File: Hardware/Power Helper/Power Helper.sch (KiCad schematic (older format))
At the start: 13 parts, among them J1 USB_C_Receptacle_Power_Only, J2 Conn_02x02_Odd_Even, J3 Conn_02x02_Odd_Even, SW1 SW_SPDT, SW2 SW_SPDT, SW3 SW_SPDT, U1 AZ1117-3.3

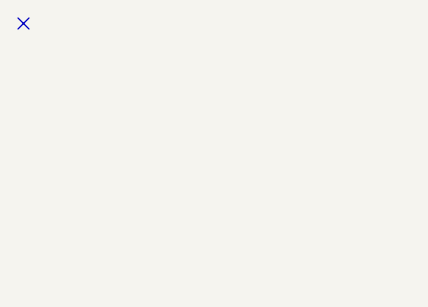
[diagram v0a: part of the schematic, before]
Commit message: JLC fix
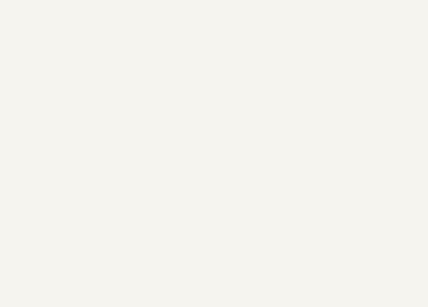
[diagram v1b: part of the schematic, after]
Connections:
- no-connect marks 2 -> 1
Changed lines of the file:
@@
 	3450 3300 3450 3400
 NoConn ~ 3450 3200
-NoConn ~ -1950 950
 $EndSCHEMATC

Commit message: Prepare for production
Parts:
- C1: LCSC (none) -> C7171
- C2: LCSC (none) -> C129272
- D1: LCSC (none) -> C2293
- J1: LCSC (none) -> C283540
- R1, R2: LCSC (none) -> C27834
- R3: LCSC (none) -> C17630
- SW1, SW2, SW3: Sparkfun (none) -> COM-10860
- U1: LCSC (none) -> C108492
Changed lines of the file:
@@
 F 2 "Power Helper:CUI_UJC-HP-3-SMT-TR" H 2100 3900 50  0001 C CNN
 F 3 "" H 2100 3900 50  0001 C CNN
+F 4 "C283540" H 1950 3900 50  0001 C CNN "LCSC"
 	1    1950 3900
 	1    0    0    -1
@@
 F 2 "Resistor_SMD:R_0805_2012Metric" V 2880 3900 50  0001 C CNN
 F 3 "~" H 2950 3900 50  0001 C CNN
+F 4 "C27834" H 2950 3900 50  0001 C CNN "LCSC"
 	1    2950 3900
 	1    0    0    -1
@@
 F 2 "Resistor_SMD:R_0805_2012Metric" V 3180 3900 50  0001 C CNN
 F 3 "~" H 3250 3900 50  0001 C CNN
+F 4 "C27834" H 3250 3900 50  0001 C CNN "LCSC"
 	1    3250 3900
 	1    0    0    -1
@@
 F 2 "Resistor_SMD:R_0805_2012Metric" V 3630 3900 50  0001 C CNN
 F 3 "~" H 3700 3900 50  0001 C CNN
+F 4 "C17630" H 3700 3900 50  0001 C CNN "LCSC"
 	1    3700 3900
 	1    0    0    -1
@@
 F 2 "LED_SMD:LED_0805_2012Metric" H 3700 3550 50  0001 C CNN
 F 3 "~" H 3700 3550 50  0001 C CNN
+F 4 "C2293" V 3700 3550 50  0001 C CNN "LCSC"
 	1    3700 3550
 	0    -1   -1   0
@@
 F 2 "Package_TO_SOT_SMD:SOT-223-3_TabPin2" H 4650 3500 50  0001 C CNN
 F 3 "https://www.diodes.com/assets/Datasheets/AZ1117.pdf" H 4750 3050 50  0001 C CNN
+F 4 "C108492" H 4650 3300 50  0001 C CNN "LCSC"
 	1    4650 3300
 	1    0    0    -1
@@
 F 2 "Capacitor_SMD:C_1206_3216Metric" H 4238 3750 50  0001 C CNN
 F 3 "~" H 4200 3900 50  0001 C CNN
+F 4 "C7171" H 4200 3900 50  0001 C CNN "LCSC"
 	1    4200 3900
 	1    0    0    -1
@@
 F 2 "Capacitor_SMD:C_1206_3216Metric" H 5138 3750 50  0001 C CNN
 F 3 "~" H 5100 3900 50  0001 C CNN
+F 4 "C129272" H 5100 3900 50  0001 C CNN "LCSC"
 	1    5100 3900
 	1    0    0    -1
@@
 F 2 "Switches:SWITCH_SPST_SMD_A" H 7550 3400 50  0001 C CNN
 F 3 "~" H 7550 3400 50  0001 C CNN
+F 4 "COM-10860" H 7550 3400 50  0001 C CNN "Sparkfun"
 	1    7550 3400
 	-1   0    0    -1
@@
 F 2 "Switches:SWITCH_SPST_SMD_A" H 7550 4000 50  0001 C CNN
 F 3 "~" H 7550 4000 50  0001 C CNN
+F 4 "COM-10860" H 7550 4000 50  0001 C CNN "Sparkfun"
 	1    7550 4000
 	-1   0    0    -1
@@
 F 2 "Switches:SWITCH_SPST_SMD_A" H 3250 3300 50  0001 C CNN
 F 3 "~" H 3250 3300 50  0001 C CNN
+F 4 "COM-10860" H 3250 3300 50  0001 C CNN "Sparkfun"
 	1    3250 3300
 	1    0    0    1
